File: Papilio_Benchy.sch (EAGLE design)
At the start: 121 parts, among them IC1 FT2232H, SW1 SWITCH-2CH-6P-3010010P1, SW2 EVQQ2, T100 MOSFET-NCHANNELSMD, U1 ARDUINO_MEGA_SHIELD, U100 PCA9306, U101 ATMEGA32U4-XUMU, U2 LTC3419EMS, U3 93C46B, X1 12MHz, Y1 16MHz KX-7

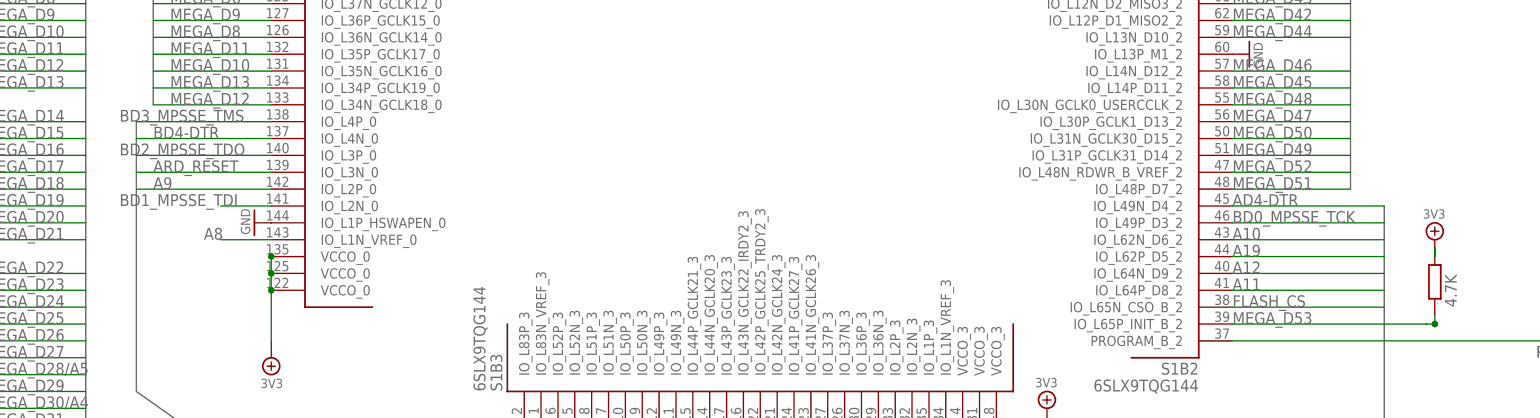
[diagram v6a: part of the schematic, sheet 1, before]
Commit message: Increased size of power and ground traces on USB connectors.
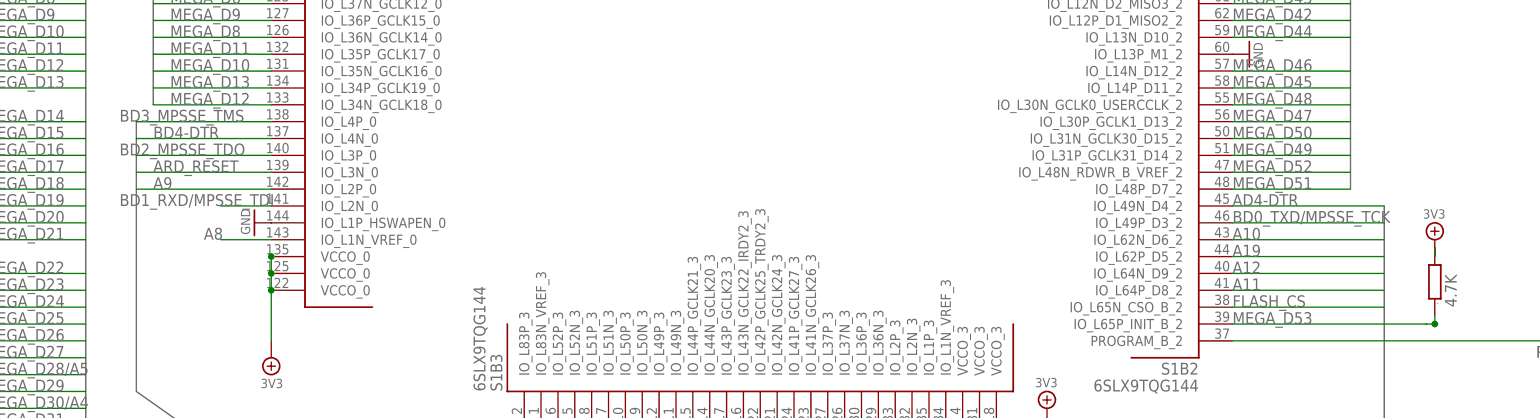
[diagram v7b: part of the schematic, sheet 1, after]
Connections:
- net BD0_MPSSE_TCK renamed BD0_TXD/MPSSE_TCK
- net BD1_MPSSE_TDI renamed BD1_RXD/MPSSE_TDI
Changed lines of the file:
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@@
 </segment>
 </net>
-<net name="BD0_MPSSE_TCK" class="0">
+<net name="BD0_TXD/MPSSE_TCK" class="0">
 <segment>
 <wire x1="205.74" y1="81.28" x2="182.88" y2="81.28" width="0.1524" layer="91"/>
@@
 </segment>
 </net>
-<net name="BD1_MPSSE_TDI" class="0">
+<net name="BD1_RXD/MPSSE_TDI" class="0">
 <segment>
 <wire x1="30.48" y1="83.82" x2="38.1" y2="83.82" width="0.1524" layer="91"/>
@@
 </segment>
 </net>
-<net name="BD1_MPSSE_TDI" class="0">
+<net name="BD1_RXD/MPSSE_TDI" class="0">
 <segment>
 <wire x1="185.42" y1="96.52" x2="195.58" y2="96.52" width="0.1524" layer="91"/>
@@
 </segment>
 </net>
-<net name="BD0_MPSSE_TCK" class="0">
+<net name="BD0_TXD/MPSSE_TCK" class="0">
 <segment>
 <wire x1="185.42" y1="99.06" x2="195.58" y2="99.06" width="0.1524" layer="91"/>

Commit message: Fix missing pin 43 on AVR.
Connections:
- net CS renamed !CS
- net OE renamed !OE
- net SW0 renamed SW1
- net WE renamed !WE
- removed net AGND: U101.GND3
- removed net ATMEGA_RXLED: U101.(SS/PCINT0)PB0
- removed net ATMEGA_TXLED: U101.(XCK1/#CTS)PD5
- net GND: now also U101.GND3
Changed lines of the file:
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@@
 </segment>
 </net>
-<net name="WE" class="0">
+<net name="!WE" class="0">
 <segment>
 <wire x1="308.61" y1="45.72" x2="306.07" y2="48.26" width="0.1524" layer="91"/>
@@
 </segment>
 </net>
-<net name="OE" class="0">
+<net name="!OE" class="0">
 <segment>
 <wire x1="308.61" y1="43.18" x2="306.07" y2="45.72" width="0.1524" layer="91"/>
@@
 </segment>
 </net>
-<net name="CS" class="0">
+<net name="!CS" class="0">
 <segment>
 <wire x1="308.61" y1="48.26" x2="306.07" y2="50.8" width="0.1524" layer="91"/>
@@
 </segment>
 </net>
-<net name="SW0" class="0">
+<net name="SW1" class="0">
 <segment>
 <pinref part="S1" gate="B1" pin="IO_L1N_VREF_1"/>
@@
 <pinref part="U$40" gate="G$1" pin="COM"/>
 <pinref part="C101" gate="G$1" pin="2"/>
+<wire x1="-7.62" y1="124.46" x2="-38.1" y2="124.46" width="0.1524" layer="91"/>
+<label x="-35.56" y="124.46" size="1.778" layer="95"/>
+<pinref part="U101" gate="G$1" pin="GND3"/>
+<wire x1="-38.1" y1="124.46" x2="-38.1" y2="129.54" width="0.1524" layer="91"/>
+<wire x1="-38.1" y1="129.54" x2="-40.64" y2="129.54" width="0.1524" layer="91"/>
 </segment>
 <segment>
@@
 </segment>
 </net>
-<net name="AGND" class="0">
-<segment>
-<wire x1="-7.62" y1="124.46" x2="-38.1" y2="124.46" width="0.1524" layer="91"/>
-<label x="-35.56" y="124.46" size="1.778" layer="95"/>
-<pinref part="U101" gate="G$1" pin="GND3"/>
-</segment>
-</net>
-<net name="ATMEGA_RXLED" class="0">
-<segment>
-<wire x1="53.34" y1="109.22" x2="71.12" y2="109.22" width="0.1524" layer="91"/>
-<label x="63.5" y="109.22" size="1.778" layer="95"/>
-<pinref part="U101" gate="G$1" pin="(SS/PCINT0)PB0"/>
-</segment>
-</net>
 <net name="ATMEGA_IO13*" class="0">
 <segment>
@@
 </segment>
 </net>
-<net name="ATMEGA_TXLED" class="0">
-<segment>
-<wire x1="71.12" y1="81.28" x2="53.34" y2="81.28" width="0.1524" layer="91"/>
-<label x="63.5" y="81.28" size="1.778" layer="95"/>
-<pinref part="U101" gate="G$1" pin="(XCK1/#CTS)PD5"/>
-</segment>
-</net>
